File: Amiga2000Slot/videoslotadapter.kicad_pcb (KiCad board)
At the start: 2 copper layers, 152 x 57.6 mm, 22 parts, among them U1 74LVC86, U2 74LVC574, U3 74LVC574, U4 TLV74333PDBVR, U5 74LVC86

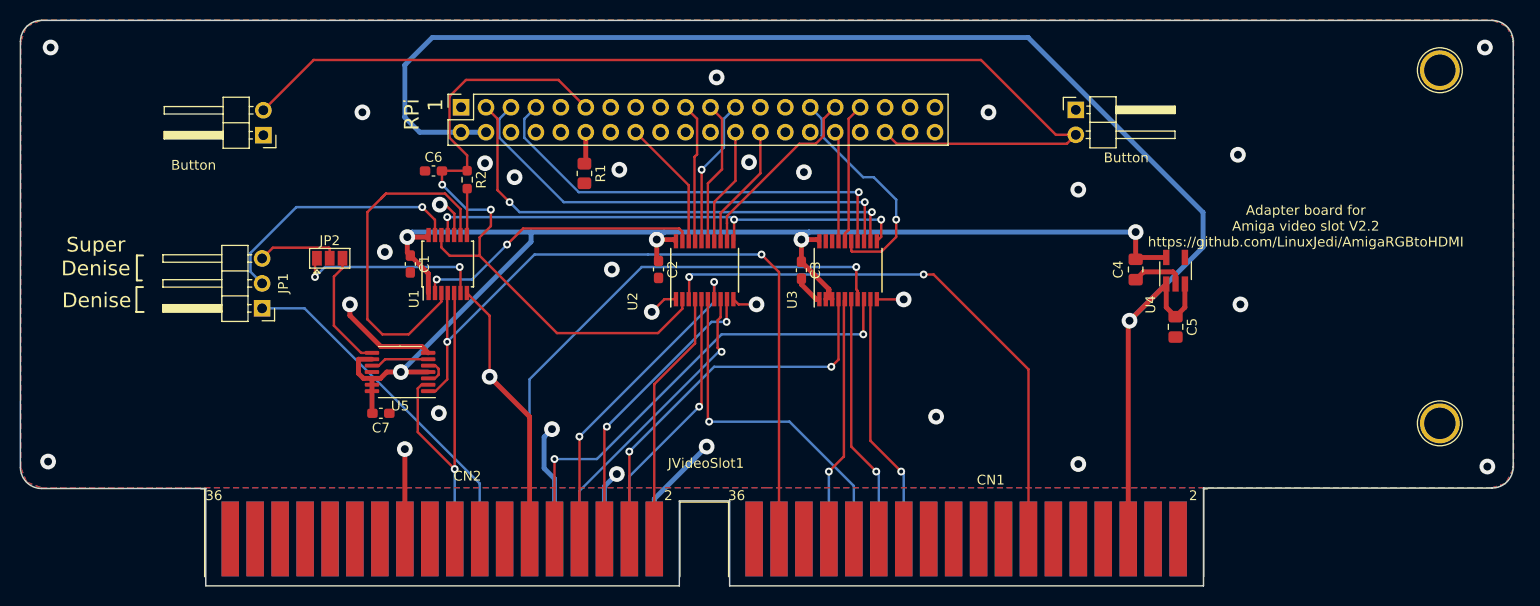
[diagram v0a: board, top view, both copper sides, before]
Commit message: A2000SlotV3 initial dump
* Strip out most of the options since we have a pretty stable build now.
* Add the mounting holes to the schematic and use M3s (need to check
  positioning later)

Note: At this stage this has not been built and there may be dragons.
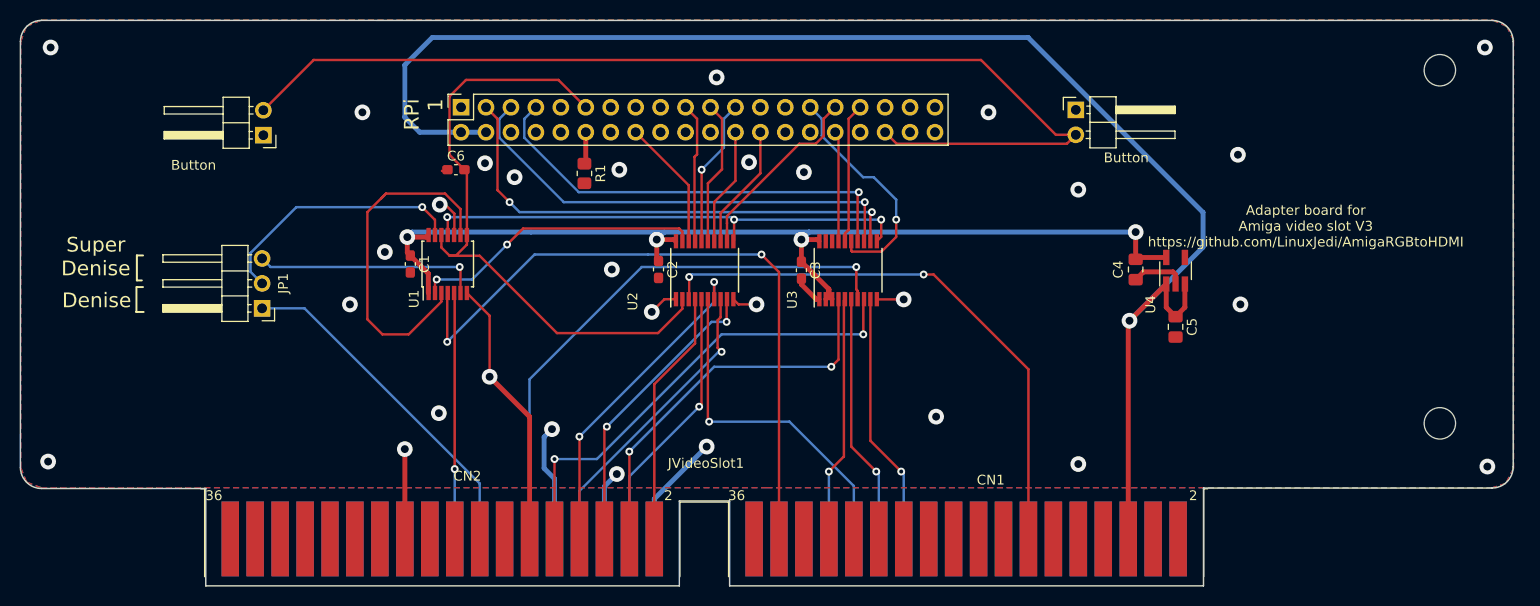
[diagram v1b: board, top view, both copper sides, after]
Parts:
- removed C7: 100nF, Capacitor_SMD:C_0603_1608Metric_Pad1.08x0.95mm_HandSolder
- removed JP2: Jumper_3_Bridged12, Jumper:SolderJumper-3_P1.3mm_Open_Pad1.0x1.5mm
- removed R2: 0R, Resistor_SMD:R_0603_1608Metric_Pad0.98x0.95mm_HandSolder
- removed U5: 74LVC86, Package_SO:TSSOP-14_4.4x5mm_P0.65mm
- H1, H2: renamed from REF**; value 1pin -> MountingHole; footprint Connectors:1pin -> MountingHole:MountingHole_3.2mm_M3_ISO14580
- moved C6 2.29 mm to (136.0, 74.7)
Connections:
- U1 pad 6: Net-(JP2-Pad1) -> Net-(JP1-Pad3)
- U1 pad 8: Net-(R2-Pad2) -> /PiCLK
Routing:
- net +3V3: track 139.6 -> 105.9 mm, vias 5 -> 4
- net Net-(JP2-Pad1): track 19.8 -> 0.00 mm, vias 2 -> 0
- net Net-(JP1-Pad3): track 8.37 -> 23.2 mm, vias 0 -> 1
- net /OPTCLK: track 12.2 -> 0.00 mm
- net /C3: track 36.1 -> 25.1 mm
- net GND: track 99.0 -> 88.4 mm
- net /C1: track 76.6 -> 70.4 mm
- net Net-(U5-Pad10): track 5.99 -> 0.00 mm
- net /PiCLK: track 70.6 -> 65.2 mm, vias 2 -> 0
- net Net-(R2-Pad2): track 4.73 -> 0.00 mm
- net Net-(U5-Pad3): track 3.02 -> 0.00 mm
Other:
- board text added: "Adapter board for Amiga video slot V3 https://github.com/LinuxJedi/AmigaRGBtoHDMI"
- board text removed: "Adapter board for Amiga video slot V2.2 https://github.com/LinuxJedi/AmigaRGBtoHDMI"
